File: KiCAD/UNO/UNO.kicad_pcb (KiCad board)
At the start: 2 copper layers, 68.6 x 53.3 mm, 18 parts, among them J1 Conn_01x03, J10 Conn_01x06, J2 Conn_01x03, J3 Conn_01x03, J4 Conn_01x03, J5 Conn_01x03, J6 Conn_01x03, J7 Conn_01x03, J8 Conn_01x03, J9 Conn_01x03, P1 Power, P2 Analog, P3 Digital, P4 Digital, P5 CONN_01X01, P6 CONN_01X01, P7 CONN_01X01, P8 CONN_01X01

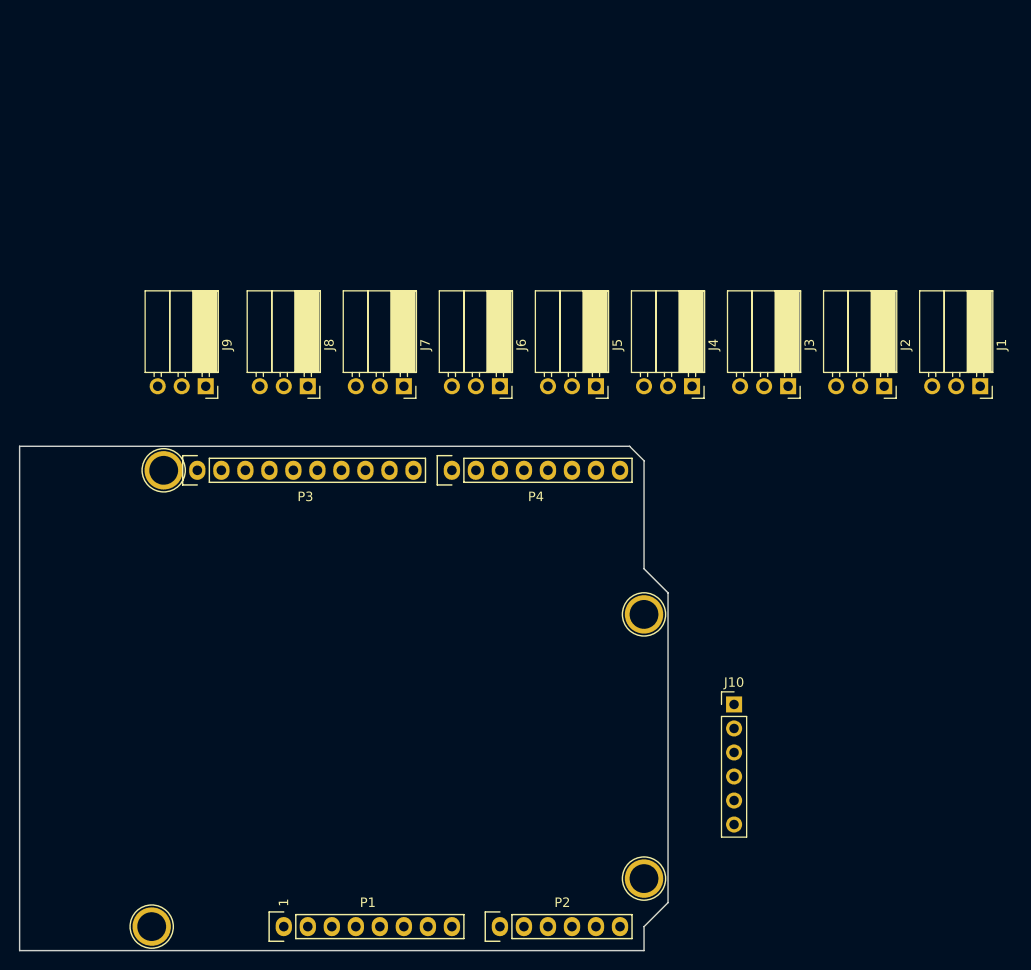
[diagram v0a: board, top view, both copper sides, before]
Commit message: More connctors added
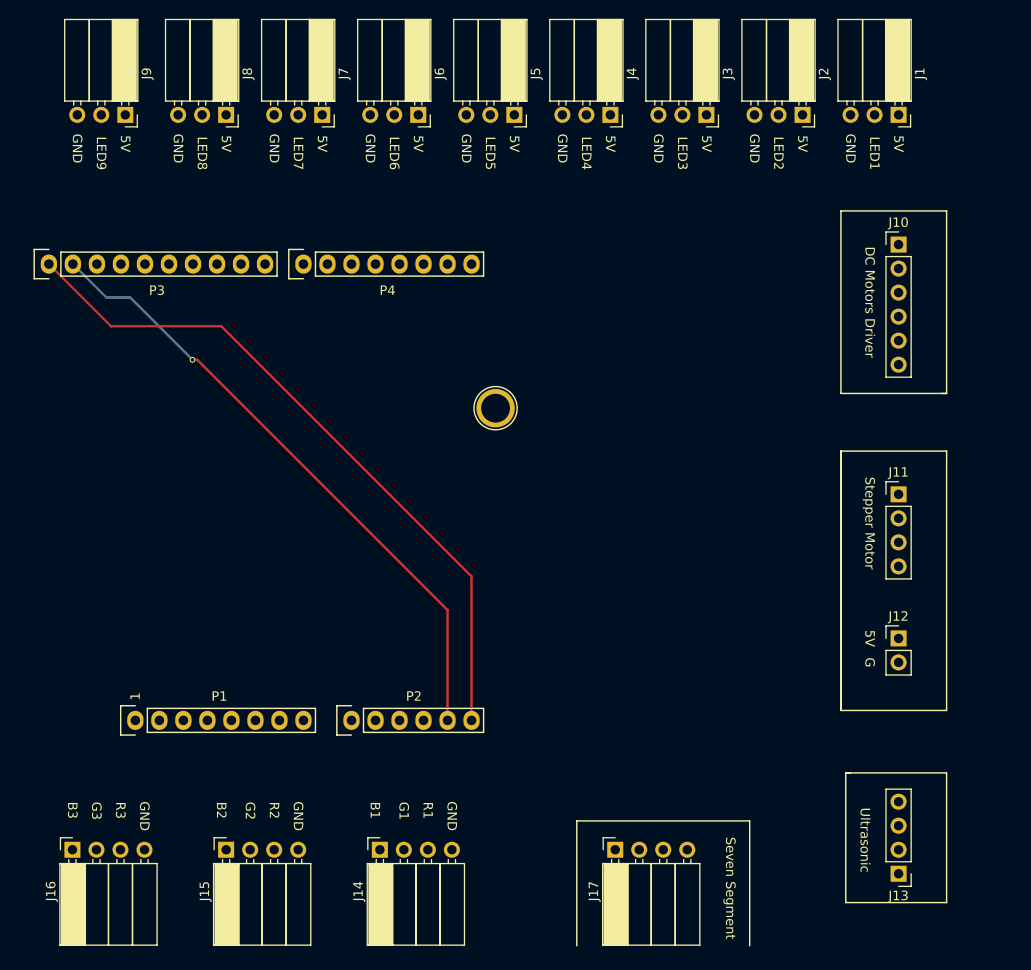
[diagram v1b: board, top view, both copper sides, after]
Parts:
- removed P5, P6, P7: CONN_01X01, Socket_Arduino_Uno:Arduino_1pin
- added J11: Conn_01x04, Socket_Strips:Socket_Strip_Straight_1x04_Pitch2.54mm, F.Cu at (204.0, 78.1)
- added J12: Conn_01x02, Socket_Strips:Socket_Strip_Straight_1x02_Pitch2.54mm, F.Cu at (204.0, 93.3)
- added J13: Conn_01x04, Socket_Strips:Socket_Strip_Straight_1x04_Pitch2.54mm, F.Cu at (204.0, 118.2)
- added J14: Conn_01x04, Socket_Strips:Socket_Strip_Angled_1x04_Pitch2.54mm, F.Cu at (149.1, 115.7)
- added J15: Conn_01x04, Socket_Strips:Socket_Strip_Angled_1x04_Pitch2.54mm, F.Cu at (132.8, 115.7)
- added J16: Conn_01x04, Socket_Strips:Socket_Strip_Angled_1x04_Pitch2.54mm, F.Cu at (116.6, 115.7)
- added J17: Conn_01x04, Socket_Strips:Socket_Strip_Angled_1x04_Pitch2.54mm, F.Cu at (174.0, 115.7)
- moved J10 51.7 mm to (204.0, 51.7)
- moved J1 30.0 mm to (204.0, 38.0)
- moved J2 30.0 mm to (193.8, 38.0)
- moved J3 30.0 mm to (183.6, 38.0)
- moved J4 30.0 mm to (173.5, 38.0)
- moved J5 30.0 mm to (163.3, 38.0)
- moved J6 30.0 mm to (153.2, 38.0)
- moved J7 30.0 mm to (143.0, 38.0)
- moved J8 30.0 mm to (132.8, 38.0)
- moved J9 29.9 mm to (122.2, 38.0)
- moved P8 26.9 mm to (161.3, 69.0)
- moved P3 26.9 mm to (114.1, 53.8)
- moved P1 26.9 mm to (123.2, 102.0)
- moved P2 26.9 mm to (146.1, 102.0)
- moved P4 26.9 mm to (141.0, 53.8)
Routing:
- net /A5(SCL): track 0.00 -> 73.6 mm
- net /A4(SDA): track 0.00 -> 66.5 mm, vias 0 -> 1
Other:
- board outline removed
- board text added: "5V"
- board text added: "B1"
- board text added: "B2"
- board text added: "B3"
- board text added: "DC Motors Driver"
- board text added: "G"
- board text added: "G1"
- board text added: "G2"
- board text added: "G3"
- board text added: "GND"
- board text added: "LED1"
- board text added: "LED2"
- board text added: "LED3"
- board text added: "LED4"
- board text added: "LED5"
- board text added: "LED6"
- board text added: "LED7"
- board text added: "LED8"
- board text added: "LED9"
- board text added: "R1"
- board text added: "R2"
- board text added: "R3"
- board text added: "Seven Segment"
- board text added: "Stepper Motor"
- board text added: "Ultrasonic"
